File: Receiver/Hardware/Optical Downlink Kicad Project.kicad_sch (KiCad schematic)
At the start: 31 parts, among them J1 Conn_01x08_Pin, U1 OPA657U, U2 TLE2426-EP_D_8, U3 OPA657U, U4 ADS8691IPWR, U5 MAX743CWE+, U6 TPS7A4700RGWT

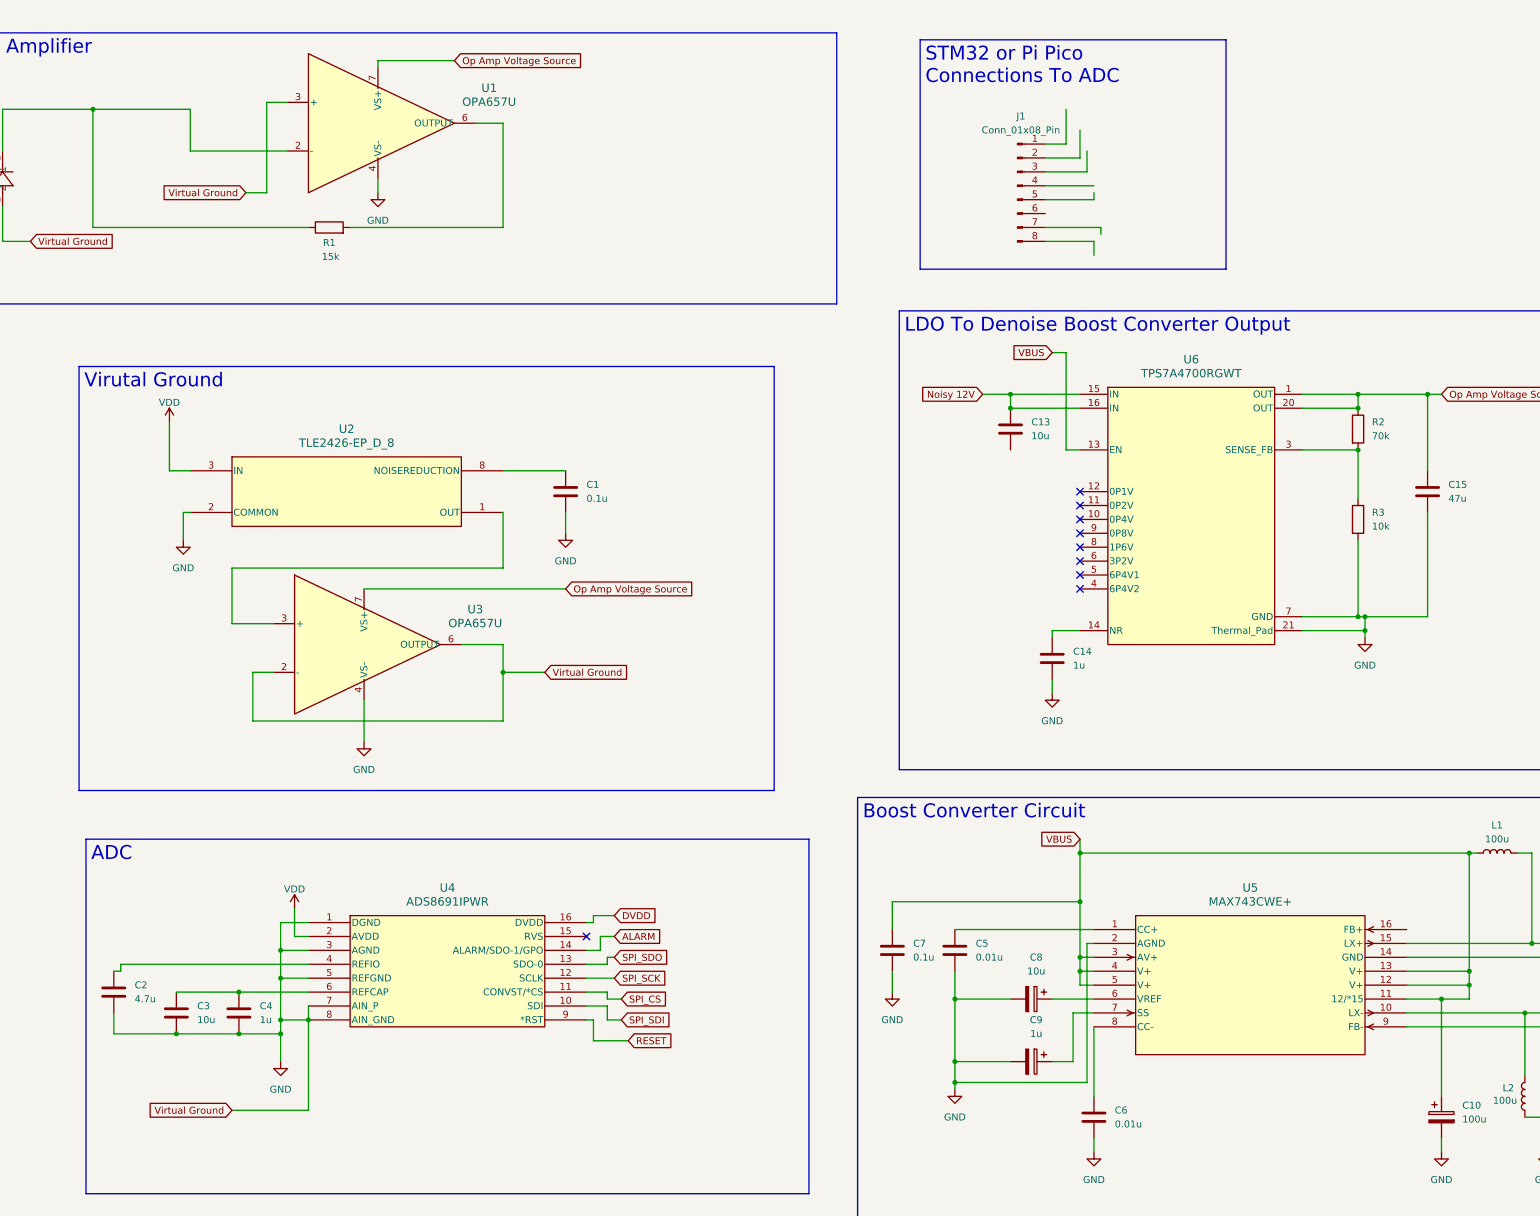
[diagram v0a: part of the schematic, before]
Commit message: Fixed issues with signal and power flags in Schematic
Fixed a issue with the signal not being wired to ADC properly, also fixed a issue where multiple flags were used for the digital power.
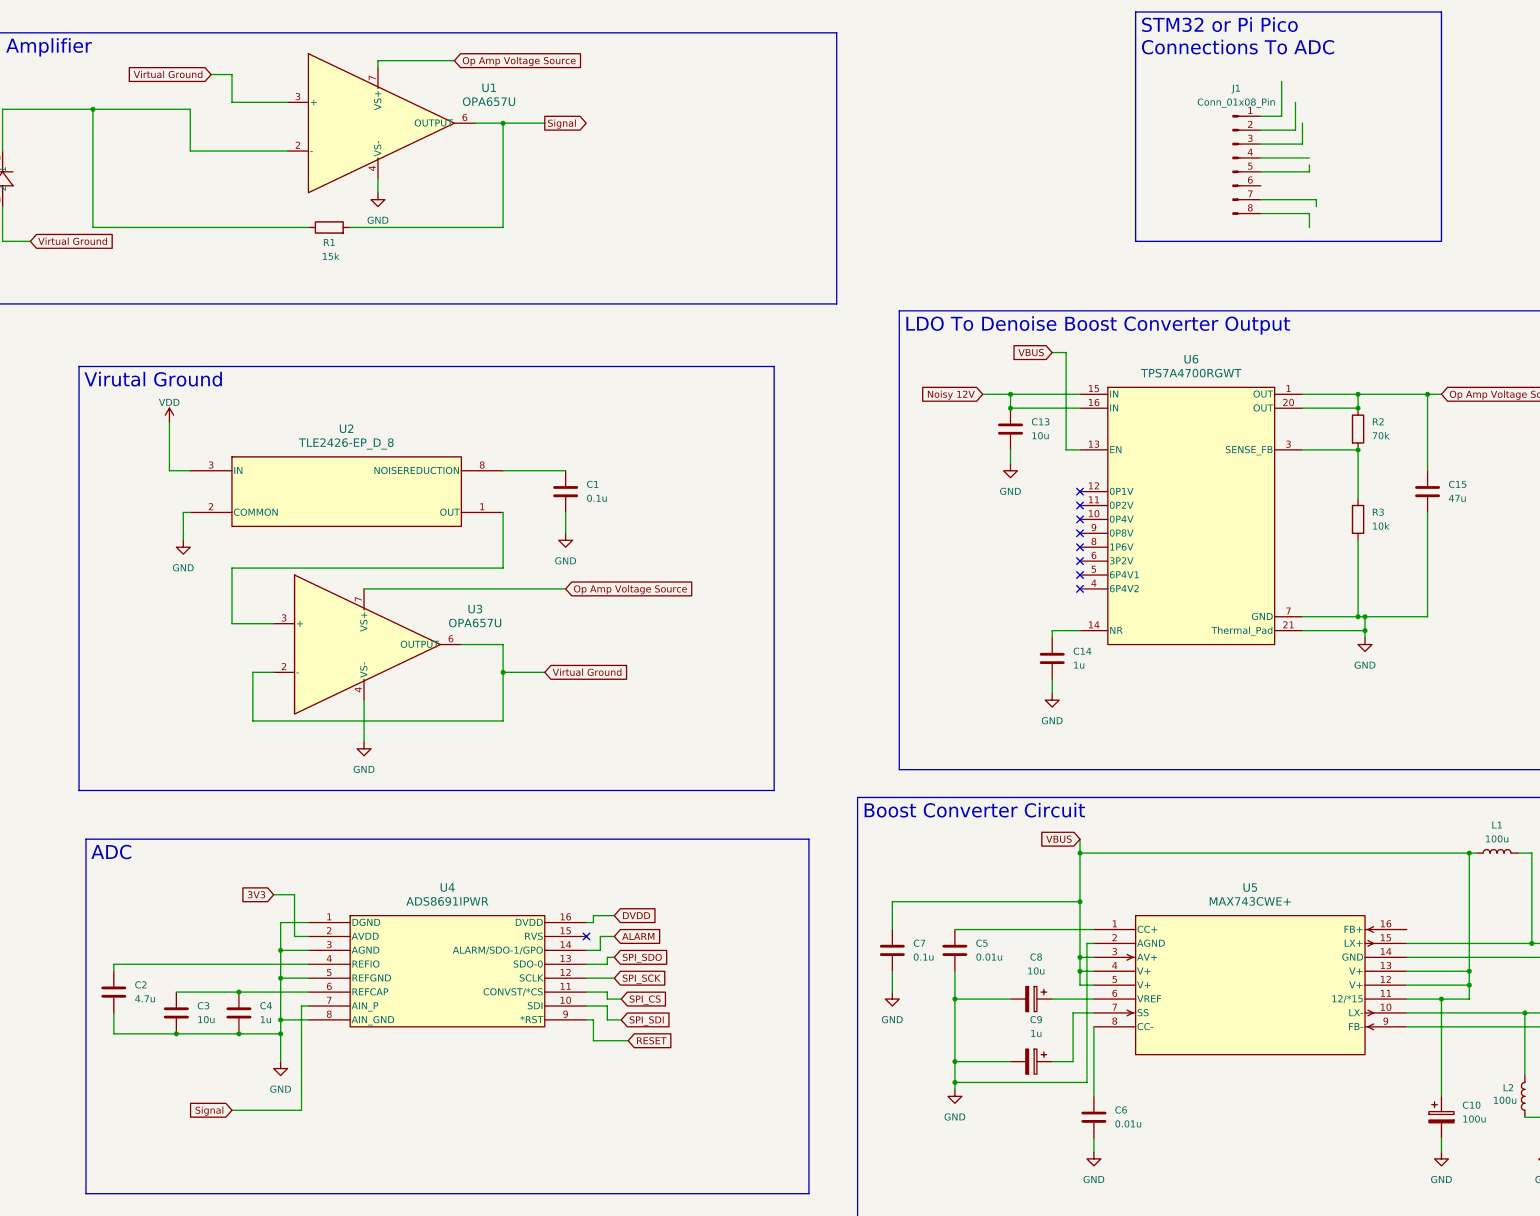
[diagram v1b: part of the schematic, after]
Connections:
- net 3V3: now also U4.2 (AVDD)
- net GND: now also C13.2; no longer CR1.2, U1.3 (+), U3.2 (-), U3.6 (OUTPUT), U4.7 (AIN_P)
- net VDD: no longer U4.2 (AVDD)
- net Signal: now reaches R1.2, U1.6 (OUTPUT)
- net Signal: now also U4.7 (AIN_P)
- new net Virtual Ground: CR1.2, U1.3 (+), U3.2 (-), U3.6 (OUTPUT)
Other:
- moved on the sheet: J1

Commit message: Added some symbols to the library.
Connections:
- net Noisy 12V: now also U5.16 (FB+)
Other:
- note added: "Note to self: Remember to switch out boost system for components Aaryan sent you. Find the symbol library stuff"
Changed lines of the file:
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@@
 	(generator_version "9.0")
 	(paper "A2")
+	(text "Note to self:\nRemember to switch out boost system for components Aaryan sent you.\nFind the symbol library stuff\n"
+		(exclude_from_sim no)
+		(at 321.818 265.43 0)
+		(effects
+			(font
+				(size 7.62 7.62)
+			)
+		)
+	)
 	(text_box "LDO To Denoise Boost Converter Output"
 		(exclude_from_sim no)
@@
 		(color 0 0 0 0)
 	)
+	(junction
+		(at 346.71 184.15)
+		(diameter 0)
+		(color 0 0 0 0)
+	)
 	(no_connect
 		(at 245.11 114.3)
@@
 	(wire
 		(pts
+			(xy 346.71 184.15) (xy 351.79 184.15)
+		)
+		(stroke
+			(width 0)
+			(type default)
+		)
+	)
+	(wire
+		(pts
 			(xy 278.13 48.26) (xy 288.29 48.26)
 		)
@@
 	(wire
 		(pts
+			(xy 325.12 175.26) (xy 346.71 175.26)
+		)
+		(stroke
+			(width 0)
+			(type default)
+		)
+	)
+	(wire
+		(pts
 			(xy 154.94 187.96) (xy 158.75 187.96)
 		)
@@
 	(wire
 		(pts
+			(xy 325.12 181.61) (xy 325.12 175.26)
+		)
+		(stroke
+			(width 0)
+			(type default)
+		)
+	)
+	(wire
+		(pts
 			(xy 285.75 127) (xy 297.18 127)
 		)
@@
 	(wire
 		(pts
+			(xy 346.71 175.26) (xy 346.71 184.15)
+		)
+		(stroke
+			(width 0)
+			(type default)
+		)
+	)
+	(wire
+		(pts
 			(xy 285.75 34.29) (xy 285.75 38.1)
 		)
@@
 	(wire
 		(pts
+			(xy 304.8 181.61) (xy 325.12 181.61)
+		)
+		(stroke
+			(width 0)
+			(type default)
+		)
+	)
+	(wire
+		(pts
 			(xy 99.06 180.34) (xy 99.06 185.42)
 		)
@@
 	(wire
 		(pts
-			(xy 337.82 184.15) (xy 351.79 184.15)
-		)
-		(stroke
+			(xy 337.82 184.15) (xy 346.71 184.15)
+		)
+		(stroke

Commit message: Changed LDO and Boost Converter
The Max743 was switched out for the MEV3S0509SC so that it the 5V is converted to 9V instead of 12V by the DC-DC converter. The TPS7A4700 was replaced with the LM2940IMPX-8.0/NOPB so that 9V could be brought down to 8V instead of 12V could be brought down to 11V.
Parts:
- removed C10, C11, C12: 100u, symbol Device:C_Polarized
- removed C13: 10u, symbol Device:C
- removed C15: 47u, symbol Device:C
- removed C7: 0.1u, symbol Device:C
- removed C8: 10u, symbol Device:C_Polarized
- removed C9: 1u, symbol Device:C_Polarized
- removed D1, D2: D_Schottky, symbol Device:D_Schottky
- removed J1: Conn_01x08_Pin, symbol Connector:Conn_01x08_Pin
- removed L2: 100u, symbol Device:L
- removed R2: 70k, symbol Device:R
- removed R3: 10k, symbol Device:R
- removed U5: MAX743CWE+, 21-0042B_16, symbol 00-symbol_library:MAX743CWE+
- removed U6: TPS7A4700RGWT, RGW0020A-IPC_A, symbol 00-symbol_library:TPS7A4700RGWT
- added U5: MEV3S0515SC, DC_MEV3_7P65X19P65_MUR, symbol 00-symbol_library:MEV3S0515SC
- added U6: LM2940IMPX-8.0/NOPB, DCY0004A_N, symbol 00-symbol_library:LM2940IMPX-8.0_NOPB
- C14: value 1u -> 2.2u
- C5: value 0.01u -> 0.47u
- C6: value 0.01u -> 22u
- L1: value 100u -> 22u
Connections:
- net GND: now also U5.2 (-VIN), U5.5 (-VOUT), U6.2 (GND), U6.4 (GND)
- net VBUS: now also U5.1 (+VIN); no longer L1.1
- net at L1.2: now also C14.1
- net at C5.1: now also U6.1 (IN)
- net at C6.1: now also U6.3 (OUT)
- new net: L1.1, U5.7 (+VOUT)
- no-connect marks 9 -> 1
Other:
- note added: "This is the symbol for the MEV3S0515SC but it has the exact same layput as MEV3S0509SC. The MEVS0509SC is the component this design will actually use."
- note removed: "Note to self: Remember to switch out boost system for components Aaryan sent you. Find the symbol library stuff"
- moved on the sheet: A1, C14

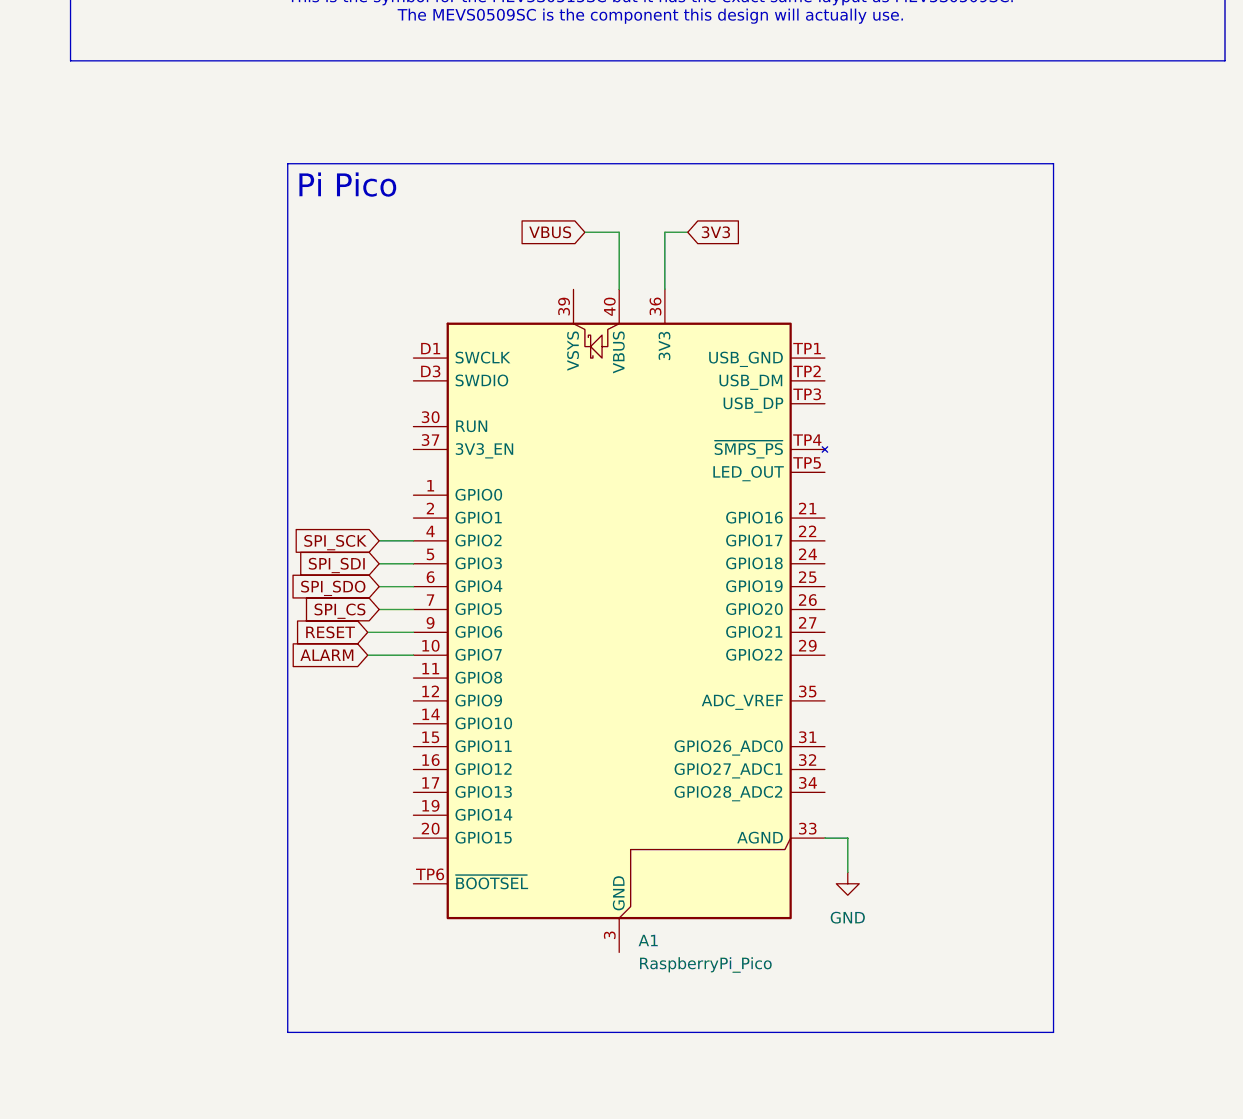
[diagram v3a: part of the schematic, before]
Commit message: Cleaned up Schematic and began placing Footprints
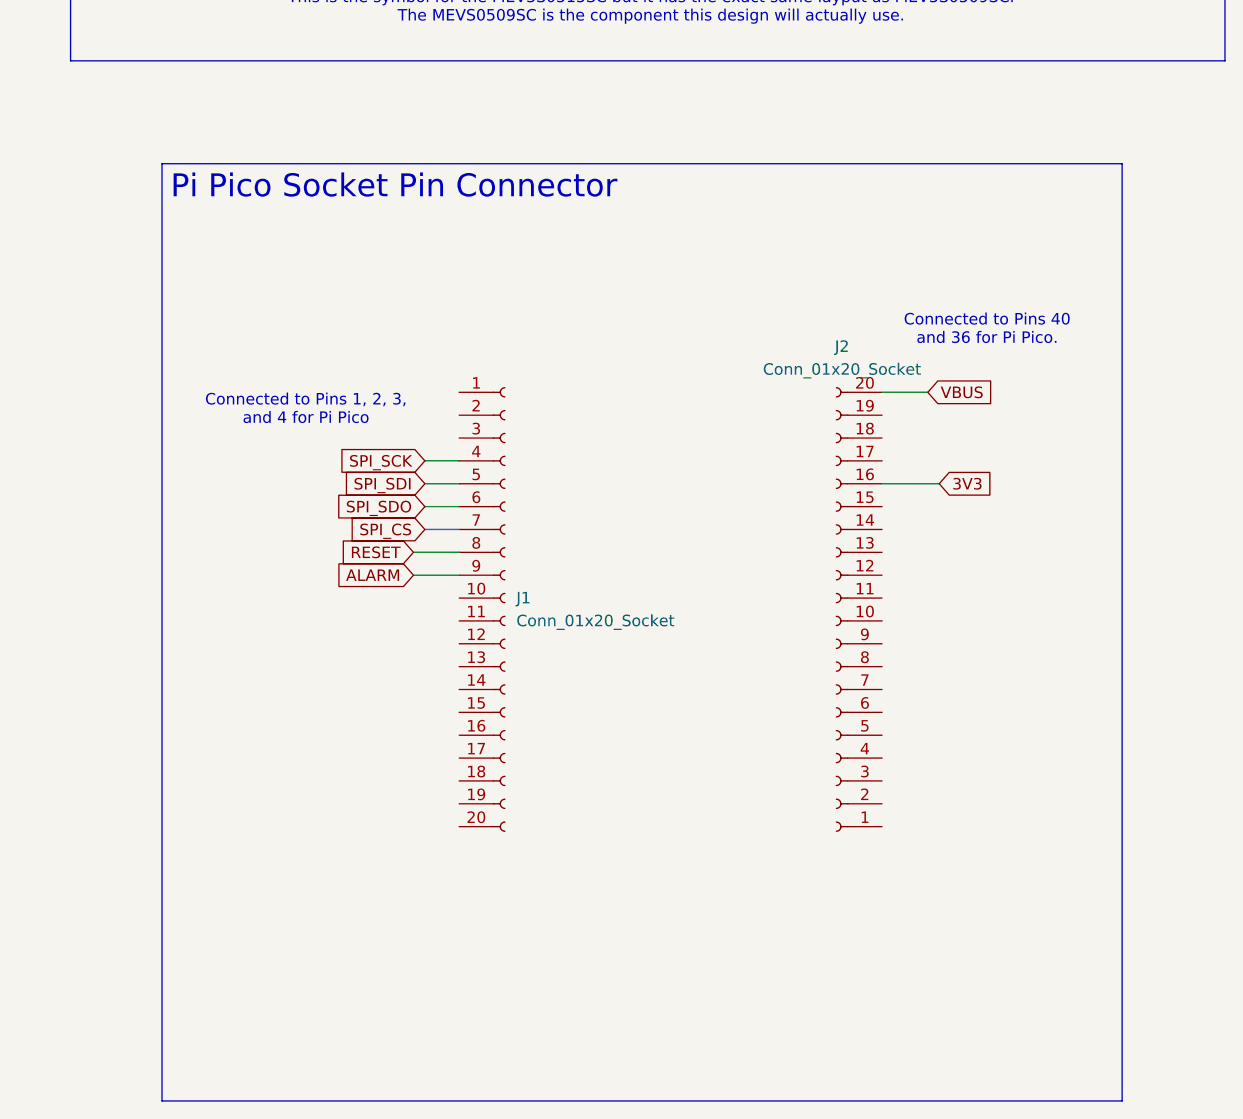
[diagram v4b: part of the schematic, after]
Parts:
- removed A1: RaspberryPi_Pico, Module:RaspberryPi_Pico_SMD, symbol MCU_Module:RaspberryPi_Pico_Extensive
- added J1, J2: Conn_01x20_Socket, Connector_PinHeader_2.54mm:PinHeader_1x20_P2.54mm_Vertical, symbol Connector:Conn_01x20_Socket
- C1, C14, C2, C3, C4, C5, C6: footprint (none) -> Capacitor_SMD:CP_Elec_3x5.3
- CR1: footprint FR4_C30737MH_EXT -> 00-footprint-library:FR4_C30737MH_EXT
- L1: footprint (none) -> Inductor_SMD:L_6.3x6.3_H3
- R1: footprint (none) -> Resistor_SMD:R_0201_0603Metric
- U1, U3: footprint D8 -> 00-footprint-library:OPA 657 D8
- U2: footprint D8_TEX -> 00-footprint-library:D8_TEX TLE2426-EP_D_8
- U4: footprint PW16_TEX -> 00-footprint-library:ADS8691IPWR_TEX
- U5: footprint DC_MEV3_7P65X19P65_MUR -> 00-footprint-library:DC_MEV3_7P65X19P65_MUR
- U6: footprint DCY0004A_N -> 00-footprint-library:LM2940IMPX-8.0_NOPB DCY0004A_N
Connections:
- net 3V3: now also J2.16 (Pin_16)
- net ALARM: now also J1.9 (Pin_9)
- net RESET: now also J1.8 (Pin_8)
- net SPI_CS: now also J1.7 (Pin_7)
- net SPI_SCK: now also J1.4 (Pin_4)
- net SPI_SDI: now also J1.5 (Pin_5)
- net SPI_SDO: now also J1.6 (Pin_6)
- net VBUS: now also J2.20 (Pin_20)
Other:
- note added: "Connected to Pins 1, 2, 3, and 4 for Pi Pico"
- note added: "Connected to Pins 40 and 36 for Pi Pico."

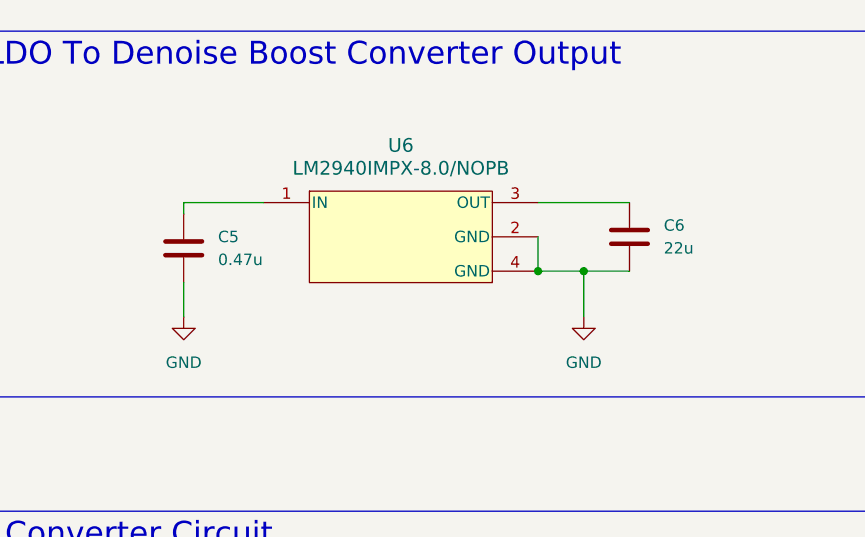
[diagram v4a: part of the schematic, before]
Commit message: Made some Symbol Changes
Have to change LDO and Boost Converter to components more accessible on JLC PCB.
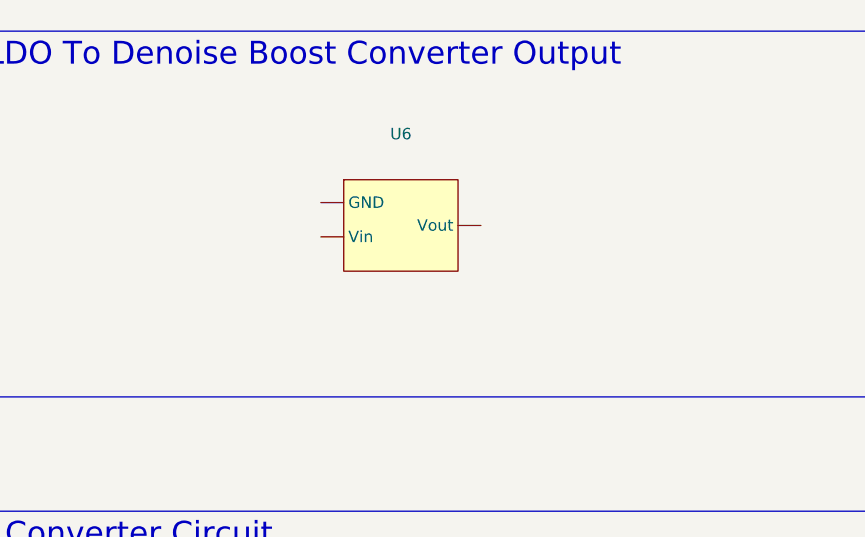
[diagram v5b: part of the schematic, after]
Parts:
- removed C5: 0.47u, Capacitor_SMD:CP_Elec_3x5.3, symbol Device:C
- removed C6: 22u, Capacitor_SMD:CP_Elec_3x5.3, symbol Device:C
- removed U6: LM2940IMPX-8.0/NOPB, 00-footprint-library:LM2940IMPX-8.0_NOPB DCY0004A_N, symbol 00-symbol_library:LM2940IMPX-8.0_NOPB
- added U6: ~, symbol 00-symbol_library:HT7580-2
